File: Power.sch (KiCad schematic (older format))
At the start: 35 parts, among them IC4 INA240A1, IC5 INA240A1, U2 IR2110S, U3 IR2110S, U4 IR2110S

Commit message: - removed 1 MOSFET of each group (no space) - removed 2 DC buffer caps (no space) - power stage routed - shunts and amps routed - post driver routed - pre driver HV routed
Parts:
- removed IC4, IC5: INA240A1, Housings_SSOP:TSSOP-8_4.4x3mm_Pitch0.65mm, symbol INA240
- removed R49, R50, R51, R52: opt, Resistors_SMD:R_0805, symbol R
- added D10, D11, D12: 3V3, Diodes_SMD:D_SOD-123, symbol ZENER
- added IC3, IC4: INA181A1, TO_SOT_Packages_SMD:SOT-23-6, symbol INA181
- added R45, R46: 10k, Resistors_SMD:R_0805, symbol R
- C40, C42: value opt -> 100n
- D5, D6, D7: value RFN2L4S -> BAS21L; footprint Diodes_SMD:SMA_Standard -> Diodes_SMD:D_SOT-23_ANK
- R47, R48: value CSS2H-3920R-L500 -> WSLF2512L5000FEB
- U2, U3, U4: footprint Housings_SOIC:SOIC-16_7.5x10.3mm_Pitch1.27mm -> Housings_SOIC:SOIC-16W_7.5x10.3mm_Pitch1.27mm
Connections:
- net labels added: U/2
- wire segments 79 -> 88
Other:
- moved on the sheet: R55, R56, R57, R58

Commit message: - fixed swapped pins 2 and 3 on IC2 - added optional dividers to ADC inputs - made Vcc selectable between 3V3 or 5V
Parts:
- D10, D11, D12: symbol ZENER -> ZENER-RESCUE-Revolter
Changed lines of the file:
@@
 $EndComp
 $Comp
-L GND-RESCUE-BLDC_4 #PWR072
+L GND-RESCUE-BLDC_4 #PWR075
 U 1 1 504F8F7B
 P 10400 1300
-F 0 "#PWR072" H 10400 1300 30  0001 C CNN
+F 0 "#PWR075" H 10400 1300 30  0001 C CNN
 F 1 "GND" H 10400 1230 30  0001 C CNN
 F 2 "" H 10400 1300 60  0001 C CNN
@@
 $EndComp
 $Comp
-L GND-RESCUE-BLDC_4 #PWR073
+L GND-RESCUE-BLDC_4 #PWR076
 U 1 1 504F8F8D
 P 10400 2000
-F 0 "#PWR073" H 10400 2000 30  0001 C CNN
+F 0 "#PWR076" H 10400 2000 30  0001 C CNN
 F 1 "GND" H 10400 1930 30  0001 C CNN
 F 2 "" H 10400 2000 60  0001 C CNN
@@
 $EndComp
 $Comp
-L GND-RESCUE-BLDC_4 #PWR074
+L GND-RESCUE-BLDC_4 #PWR077
 U 1 1 504F8FAF
 P 10400 2700
-F 0 "#PWR074" H 10400 2700 30  0001 C CNN
+F 0 "#PWR077" H 10400 2700 30  0001 C CNN
 F 1 "GND" H 10400 2630 30  0001 C CNN
 F 2 "" H 10400 2700 60  0001 C CNN
@@
 $EndComp
 $Comp
-L +12V #PWR075
+L +12V #PWR078
 U 1 1 574ED597
 P 2500 900
-F 0 "#PWR075" H 2500 750 50  0001 C CNN
+F 0 "#PWR078" H 2500 750 50  0001 C CNN
 F 1 "+12V" H 2500 1040 50  0000 C CNN
 F 2 "" H 2500 900 50  0000 C CNN
@@
 $EndComp
 $Comp
-L GND #PWR076
+L GND #PWR079
 U 1 1 574EDDD7
 P 1850 1050
-F 0 "#PWR076" H 1850 800 50  0001 C CNN
+F 0 "#PWR079" H 1850 800 50  0001 C CNN
 F 1 "GND" H 1850 900 50  0000 C CNN
 F 2 "" H 1850 1050 50  0000 C CNN
@@
 $EndComp
 $Comp
-L GND #PWR077
+L GND #PWR080
 U 1 1 574F0470
 P 2200 2300
-F 0 "#PWR077" H 2200 2050 50  0001 C CNN
+F 0 "#PWR080" H 2200 2050 50  0001 C CNN
 F 1 "GND" H 2200 2150 50  0000 C CNN
 F 2 "" H 2200 2300 50  0000 C CNN
@@
 $EndComp
 $Comp
-L +12V #PWR078
+L +12V #PWR081
 U 1 1 57504386
 P 2500 3200
-F 0 "#PWR078" H 2500 3050 50  0001 C CNN
+F 0 "#PWR081" H 2500 3050 50  0001 C CNN
 F 1 "+12V" H 2500 3340 50  0000 C CNN
 F 2 "" H 2500 3200 50  0000 C CNN
@@
 $EndComp
 $Comp
-L GND #PWR079
+L GND #PWR082
 U 1 1 5750439C
 P 1850 3350
-F 0 "#PWR079" H 1850 3100 50  0001 C CNN
+F 0 "#PWR082" H 1850 3100 50  0001 C CNN
 F 1 "GND" H 1850 3200 50  0000 C CNN
 F 2 "" H 1850 3350 50  0000 C CNN
@@
 $EndComp
 $Comp
-L GND #PWR080
+L GND #PWR083
 U 1 1 575043A3
 P 2200 4600
-F 0 "#PWR080" H 2200 4350 50  0001 C CNN
+F 0 "#PWR083" H 2200 4350 50  0001 C CNN
 F 1 "GND" H 2200 4450 50  0000 C CNN
 F 2 "" H 2200 4600 50  0000 C CNN
@@
 $EndComp
 $Comp
-L +12V #PWR081
+L +12V #PWR084
 U 1 1 57504606
 P 2450 5350
-F 0 "#PWR081" H 2450 5200 50  0001 C CNN
+F 0 "#PWR084" H 2450 5200 50  0001 C CNN
 F 1 "+12V" H 2450 5490 50  0000 C CNN
 F 2 "" H 2450 5350 50  0000 C CNN
@@
 $EndComp
 $Comp
-L GND #PWR082
+L GND #PWR085
 U 1 1 5750461C
 P 1800 5500
-F 0 "#PWR082" H 1800 5250 50  0001 C CNN
+F 0 "#PWR085" H 1800 5250 50  0001 C CNN
 F 1 "GND" H 1800 5350 50  0000 C CNN
 F 2 "" H 1800 5500 50  0000 C CNN
@@
 $EndComp
 $Comp
-L GND #PWR083
+L GND #PWR086
 U 1 1 57504623
 P 2150 6750
-F 0 "#PWR083" H 2150 6500 50  0001 C CNN
+F 0 "#PWR086" H 2150 6500 50  0001 C CNN
 F 1 "GND" H 2150 6600 50  0000 C CNN
 F 2 "" H 2150 6750 50  0000 C CNN
@@
 H2_VS
 $Comp
-L +3V3 #PWR084
+L +3V3 #PWR087
 U 1 1 575461AA
 P 2200 900
-F 0 "#PWR084" H 2200 750 50  0001 C CNN
+F 0 "#PWR087" H 2200 750 50  0001 C CNN
 F 1 "+3V3" H 2200 1040 50  0000 C CNN
 F 2 "" H 2200 900 50  0000 C CNN
@@
 $EndComp
 $Comp
-L +3V3 #PWR085
+L +3V3 #PWR088
 U 1 1 575462A0
 P 2200 3200
-F 0 "#PWR085" H 2200 3050 50  0001 C CNN
+F 0 "#PWR088" H 2200 3050 50  0001 C CNN
 F 1 "+3V3" H 2200 3340 50  0000 C CNN
 F 2 "" H 2200 3200 50  0000 C CNN
@@
 $EndComp
 $Comp
-L +3V3 #PWR086
+L +3V3 #PWR089
 U 1 1 57546CC3
 P 2150 5350
-F 0 "#PWR086" H 2150 5200 50  0001 C CNN
+F 0 "#PWR089" H 2150 5200 50  0001 C CNN
 F 1 "+3V3" H 2150 5490 50  0000 C CNN
 F 2 "" H 2150 5350 50  0000 C CNN
@@
 $EndComp
 $Comp
-L GNDPWR #PWR087
+L GNDPWR #PWR090
 U 1 1 58976189
 P 4150 2800
-F 0 "#PWR087" H 4150 2600 50  0001 C CNN
+F 0 "#PWR090" H 4150 2600 50  0001 C CNN
 F 1 "GNDPWR" H 4150 2670 50  0000 C CNN
 F 2 "" H 4150 2750 50  0000 C CNN
@@
 $EndComp
 $Comp
-L GND-RESCUE-BLDC_4 #PWR088
+L GND-RESCUE-BLDC_4 #PWR091
 U 1 1 5897662E
 P 5050 3000
-F 0 "#PWR088" H 5050 3000 30  0001 C CNN
+F 0 "#PWR091" H 5050 3000 30  0001 C CNN
 F 1 "GND" H 5050 2930 30  0001 C CNN
 F 2 "" H 5050 3000 60  0001 C CNN
@@
 $EndComp
 $Comp
-L +3V3 #PWR089
+L +3V3 #PWR092
 U 1 1 58977A83
 P 4450 1850
-F 0 "#PWR089" H 4450 1700 50  0001 C CNN
+F 0 "#PWR092" H 4450 1700 50  0001 C CNN
 F 1 "+3V3" H 4450 1990 50  0000 C CNN
 F 2 "" H 4450 1850 50  0000 C CNN
@@
 $EndComp
 $Comp
-L GND-RESCUE-BLDC_4 #PWR090
+L GND-RESCUE-BLDC_4 #PWR093
 U 1 1 58978042
 P 4450 2150
-F 0 "#PWR090" H 4450 2150 30  0001 C CNN
+F 0 "#PWR093" H 4450 2150 30  0001 C CNN
 F 1 "GND" H 4450 2080 30  0001 C CNN
 F 2 "" H 4450 2150 60  0001 C CNN
@@
 $EndComp
 $Comp
-L GND-RESCUE-BLDC_4 #PWR091
+L GND-RESCUE-BLDC_4 #PWR094
 U 1 1 589781C4
 P 4700 2150
-F 0 "#PWR091" H 4700 2150 30  0001 C CNN
+F 0 "#PWR094" H 4700 2150 30  0001 C CNN
 F 1 "GND" H 4700 2080 30  0001 C CNN
 F 2 "" H 4700 2150 60  0001 C CNN
@@
 $EndComp
 $Comp
-L GNDPWR #PWR092
+L GNDPWR #PWR095
 U 1 1 58979499
 P 4100 7250
-F 0 "#PWR092" H 4100 7050 50  0001 C CNN
+F 0 "#PWR095" H 4100 7050 50  0001 C CNN
 F 1 "GNDPWR" H 4100 7120 50  0000 C CNN
 F 2 "" H 4100 7200 50  0000 C CNN
@@
 $EndComp
 $Comp
-L GND-RESCUE-BLDC_4 #PWR093
+L GND-RESCUE-BLDC_4 #PWR096
 U 1 1 589794A0
 P 5000 7450
-F 0 "#PWR093" H 5000 7450 30  0001 C CNN
+F 0 "#PWR096" H 5000 7450 30  0001 C CNN
 F 1 "GND" H 5000 7380 30  0001 C CNN
 F 2 "" H 5000 7450 60  0001 C CNN
@@
 $EndComp
 $Comp
-L +3V3 #PWR094
+L +3V3 #PWR097
 U 1 1 589794AC
 P 4400 6300
-F 0 "#PWR094" H 4400 6150 50  0001 C CNN
+F 0 "#PWR097" H 4400 6150 50  0001 C CNN
 F 1 "+3V3" H 4400 6440 50  0000 C CNN
 F 2 "" H 4400 6300 50  0000 C CNN
@@
 $EndComp
 $Comp
-L GND-RESCUE-BLDC_4 #PWR095
+L GND-RESCUE-BLDC_4 #PWR098
 U 1 1 589794BE
 P 4400 6600
-F 0 "#PWR095" H 4400 6600 30  0001 C CNN
+F 0 "#PWR098" H 4400 6600 30  0001 C CNN
 F 1 "GND" H 4400 6530 30  0001 C CNN
 F 2 "" H 4400 6600 60  0001 C CNN
@@
 $EndComp
 $Comp
-L GND-RESCUE-BLDC_4 #PWR096
+L GND-RESCUE-BLDC_4 #PWR099
 U 1 1 589794C4
 P 4650 6600
-F 0 "#PWR096" H 4650 6600 30  0001 C CNN
+F 0 "#PWR099" H 4650 6600 30  0001 C CNN
 F 1 "GND" H 4650 6530 30  0001 C CNN
 F 2 "" H 4650 6600 60  0001 C CNN
@@
 BR_SO1
 $Comp
-L GNDPWR #PWR097
+L GNDPWR #PWR0100
 U 1 1 58985697
 P 4150 4700
-F 0 "#PWR097" H 4150 4500 50  0001 C CNN
+F 0 "#PWR0100" H 4150 4500 50  0001 C CNN
 F 1 "GNDPWR" H 4150 4570 50  0000 C CNN
 F 2 "" H 4150 4650 50  0000 C CNN
@@
 $EndComp
 $Comp
-L ZENER D10
+L ZENER-RESCUE-Revolter D10
 U 1 1 599A646A
 P 9900 1550
@@
 $EndComp
 $Comp
-L ZENER D11
+L ZENER-RESCUE-Revolter D11
 U 1 1 599A6EDF
 P 9900 2250
@@
 $EndComp
 $Comp
-L ZENER D12
+L ZENER-RESCUE-Revolter D12
 U 1 1 599A735E
 P 9900 2950
@@
 Connection ~ 5750 2700
 $Comp
-L GND-RESCUE-BLDC_4 #PWR098
+L GND-RESCUE-BLDC_4 #PWR0101
 U 1 1 59A0D35D
 P 5750 3000
-F 0 "#PWR098" H 5750 3000 30  0001 C CNN
+F 0 "#PWR0101" H 5750 3000 30  0001 C CNN
 F 1 "GND" H 5750 2930 30  0001 C CNN
 F 2 "" H 5750 3000 60  0001 C CNN
@@
 $EndComp
 $Comp
-L GND-RESCUE-BLDC_4 #PWR099
+L GND-RESCUE-BLDC_4 #PWR0102
 U 1 1 59A0DC28
 P 6000 3000
-F 0 "#PWR099" H 6000 3000 30  0001 C CNN
+F 0 "#PWR0102" H 6000 3000 30  0001 C CNN
 F 1 "GND" H 6000 2930 30  0001 C CNN
 F 2 "" H 6000 3000 60  0001 C CNN
@@
 $EndComp
 $Comp
-L GND-RESCUE-BLDC_4 #PWR0100
+L GND-RESCUE-BLDC_4 #PWR0103
 U 1 1 59A0ED1B
 P 5500 7450
-F 0 "#PWR0100" H 5500 7450 30  0001 C CNN
+F 0 "#PWR0103" H 5500 7450 30  0001 C CNN
 F 1 "GND" H 5500 7380 30  0001 C CNN
 F 2 "" H 5500 7450 60  0001 C CNN

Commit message: - basis commit for V1.1 - did an great overhaul of high current paths - fixed wrong 3V3 reg pin out - blew the IO connector up to 8 pins (turns out 7pin is rare) - changed shunt to 2512 - changed hf caps to double 1210 - two input caps - pin outs for all IO on silk screen - spread the references so you can actually read them - connected the Hall/Temp pull-ups to 3V3 instead of 5V - changed vias to 0.6/0.3mm - changed text to V1.1
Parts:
- R47, R48: footprint alexmod:CSS3920 -> Resistors_SMD:R_2512
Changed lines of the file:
@@
 $EndComp
 $Comp
-L GND-RESCUE-BLDC_4 #PWR075
+L GND-RESCUE-BLDC_4 #PWR076
 U 1 1 504F8F7B
 P 10400 1300
-F 0 "#PWR075" H 10400 1300 30  0001 C CNN
+F 0 "#PWR076" H 10400 1300 30  0001 C CNN
 F 1 "GND" H 10400 1230 30  0001 C CNN
 F 2 "" H 10400 1300 60  0001 C CNN
@@
 $EndComp
 $Comp
-L GND-RESCUE-BLDC_4 #PWR076
+L GND-RESCUE-BLDC_4 #PWR077
 U 1 1 504F8F8D
 P 10400 2000
-F 0 "#PWR076" H 10400 2000 30  0001 C CNN
+F 0 "#PWR077" H 10400 2000 30  0001 C CNN
 F 1 "GND" H 10400 1930 30  0001 C CNN
 F 2 "" H 10400 2000 60  0001 C CNN
@@
 $EndComp
 $Comp
-L GND-RESCUE-BLDC_4 #PWR077
+L GND-RESCUE-BLDC_4 #PWR078
 U 1 1 504F8FAF
 P 10400 2700
-F 0 "#PWR077" H 10400 2700 30  0001 C CNN
+F 0 "#PWR078" H 10400 2700 30  0001 C CNN
 F 1 "GND" H 10400 2630 30  0001 C CNN
 F 2 "" H 10400 2700 60  0001 C CNN
@@
 $EndComp
 $Comp
-L +12V #PWR078
+L +12V #PWR079
 U 1 1 574ED597
 P 2500 900
-F 0 "#PWR078" H 2500 750 50  0001 C CNN
+F 0 "#PWR079" H 2500 750 50  0001 C CNN
 F 1 "+12V" H 2500 1040 50  0000 C CNN
 F 2 "" H 2500 900 50  0000 C CNN
@@
 $EndComp
 $Comp
-L GND #PWR079
+L GND #PWR080
 U 1 1 574EDDD7
 P 1850 1050
-F 0 "#PWR079" H 1850 800 50  0001 C CNN
+F 0 "#PWR080" H 1850 800 50  0001 C CNN
 F 1 "GND" H 1850 900 50  0000 C CNN
 F 2 "" H 1850 1050 50  0000 C CNN
@@
 $EndComp
 $Comp
-L GND #PWR080
+L GND #PWR081
 U 1 1 574F0470
 P 2200 2300
-F 0 "#PWR080" H 2200 2050 50  0001 C CNN
+F 0 "#PWR081" H 2200 2050 50  0001 C CNN
 F 1 "GND" H 2200 2150 50  0000 C CNN
 F 2 "" H 2200 2300 50  0000 C CNN
@@
 $EndComp
 $Comp
-L +12V #PWR081
+L +12V #PWR082
 U 1 1 57504386
 P 2500 3200
-F 0 "#PWR081" H 2500 3050 50  0001 C CNN
+F 0 "#PWR082" H 2500 3050 50  0001 C CNN
 F 1 "+12V" H 2500 3340 50  0000 C CNN
 F 2 "" H 2500 3200 50  0000 C CNN
@@
 $EndComp
 $Comp
-L GND #PWR082
+L GND #PWR083
 U 1 1 5750439C
 P 1850 3350
-F 0 "#PWR082" H 1850 3100 50  0001 C CNN
+F 0 "#PWR083" H 1850 3100 50  0001 C CNN
 F 1 "GND" H 1850 3200 50  0000 C CNN
 F 2 "" H 1850 3350 50  0000 C CNN
@@
 $EndComp
 $Comp
-L GND #PWR083
+L GND #PWR084
 U 1 1 575043A3
 P 2200 4600
-F 0 "#PWR083" H 2200 4350 50  0001 C CNN
+F 0 "#PWR084" H 2200 4350 50  0001 C CNN
 F 1 "GND" H 2200 4450 50  0000 C CNN
 F 2 "" H 2200 4600 50  0000 C CNN
@@
 $EndComp
 $Comp
-L +12V #PWR084
+L +12V #PWR085
 U 1 1 57504606
 P 2450 5350
-F 0 "#PWR084" H 2450 5200 50  0001 C CNN
+F 0 "#PWR085" H 2450 5200 50  0001 C CNN
 F 1 "+12V" H 2450 5490 50  0000 C CNN
 F 2 "" H 2450 5350 50  0000 C CNN
@@
 $EndComp
 $Comp
-L GND #PWR085
+L GND #PWR086
 U 1 1 5750461C
 P 1800 5500
-F 0 "#PWR085" H 1800 5250 50  0001 C CNN
+F 0 "#PWR086" H 1800 5250 50  0001 C CNN
 F 1 "GND" H 1800 5350 50  0000 C CNN
 F 2 "" H 1800 5500 50  0000 C CNN
@@
 $EndComp
 $Comp
-L GND #PWR086
+L GND #PWR087
 U 1 1 57504623
 P 2150 6750
-F 0 "#PWR086" H 2150 6500 50  0001 C CNN
+F 0 "#PWR087" H 2150 6500 50  0001 C CNN
 F 1 "GND" H 2150 6600 50  0000 C CNN
 F 2 "" H 2150 6750 50  0000 C CNN
@@
 H2_VS
 $Comp
-L +3V3 #PWR087
+L +3V3 #PWR088
 U 1 1 575461AA
 P 2200 900
-F 0 "#PWR087" H 2200 750 50  0001 C CNN
+F 0 "#PWR088" H 2200 750 50  0001 C CNN
 F 1 "+3V3" H 2200 1040 50  0000 C CNN
 F 2 "" H 2200 900 50  0000 C CNN
@@
 $EndComp
 $Comp
-L +3V3 #PWR088
+L +3V3 #PWR089
 U 1 1 575462A0
 P 2200 3200
-F 0 "#PWR088" H 2200 3050 50  0001 C CNN
+F 0 "#PWR089" H 2200 3050 50  0001 C CNN
 F 1 "+3V3" H 2200 3340 50  0000 C CNN
 F 2 "" H 2200 3200 50  0000 C CNN
@@
 $EndComp
 $Comp
-L +3V3 #PWR089
+L +3V3 #PWR090
 U 1 1 57546CC3
 P 2150 5350
-F 0 "#PWR089" H 2150 5200 50  0001 C CNN
+F 0 "#PWR090" H 2150 5200 50  0001 C CNN
 F 1 "+3V3" H 2150 5490 50  0000 C CNN
 F 2 "" H 2150 5350 50  0000 C CNN
@@
 F 0 "R48" V 4230 2550 50  0000 C CNN
 F 1 "WSLF2512L5000FEB" V 4350 2750 50  0000 C CNN
-F 2 "alexmod:CSS3920" V 4080 2550 50  0001 C CNN
+F 2 "Resistors_SMD:R_2512" V 4080 2550 50  0001 C CNN
 F 3 "" H 4150 2550 50  0000 C CNN
 	1    4150 2550
@@
 $EndComp
 $Comp
-L GNDPWR #PWR090
+L GNDPWR #PWR091
 U 1 1 58976189
 P 4150 2800
-F 0 "#PWR090" H 4150 2600 50  0001 C CNN
+F 0 "#PWR091" H 4150 2600 50  0001 C CNN
 F 1 "GNDPWR" H 4150 2670 50  0000 C CNN
 F 2 "" H 4150 2750 50  0000 C CNN
@@
 $EndComp
 $Comp
-L GND-RESCUE-BLDC_4 #PWR091
+L GND-RESCUE-BLDC_4 #PWR092
 U 1 1 5897662E
 P 5050 3000
-F 0 "#PWR091" H 5050 3000 30  0001 C CNN
+F 0 "#PWR092" H 5050 3000 30  0001 C CNN
 F 1 "GND" H 5050 2930 30  0001 C CNN
 F 2 "" H 5050 3000 60  0001 C CNN
@@
 $EndComp
 $Comp
-L +3V3 #PWR092
+L +3V3 #PWR093
 U 1 1 58977A83
 P 4450 1850
-F 0 "#PWR092" H 4450 1700 50  0001 C CNN
+F 0 "#PWR093" H 4450 1700 50  0001 C CNN
 F 1 "+3V3" H 4450 1990 50  0000 C CNN
 F 2 "" H 4450 1850 50  0000 C CNN
@@
 $EndComp
 $Comp
-L GND-RESCUE-BLDC_4 #PWR093
+L GND-RESCUE-BLDC_4 #PWR094
 U 1 1 58978042
 P 4450 2150
-F 0 "#PWR093" H 4450 2150 30  0001 C CNN
+F 0 "#PWR094" H 4450 2150 30  0001 C CNN
 F 1 "GND" H 4450 2080 30  0001 C CNN
 F 2 "" H 4450 2150 60  0001 C CNN
@@
 $EndComp
 $Comp
-L GND-RESCUE-BLDC_4 #PWR094
+L GND-RESCUE-BLDC_4 #PWR095
 U 1 1 589781C4
 P 4700 2150
-F 0 "#PWR094" H 4700 2150 30  0001 C CNN
+F 0 "#PWR095" H 4700 2150 30  0001 C CNN
 F 1 "GND" H 4700 2080 30  0001 C CNN
 F 2 "" H 4700 2150 60  0001 C CNN
@@
 F 0 "R47" V 4180 7000 50  0000 C CNN
 F 1 "WSLF2512L5000FEB" V 4350 7200 50  0000 C CNN
-F 2 "alexmod:CSS3920" V 4030 7000 50  0001 C CNN
+F 2 "Resistors_SMD:R_2512" V 4030 7000 50  0001 C CNN
 F 3 "" H 4100 7000 50  0000 C CNN
 	1    4100 7000
@@
 $EndComp
 $Comp
-L GNDPWR #PWR095
+L GNDPWR #PWR096
 U 1 1 58979499
 P 4100 7250
-F 0 "#PWR095" H 4100 7050 50  0001 C CNN
+F 0 "#PWR096" H 4100 7050 50  0001 C CNN
 F 1 "GNDPWR" H 4100 7120 50  0000 C CNN
 F 2 "" H 4100 7200 50  0000 C CNN
@@
 $EndComp
 $Comp
-L GND-RESCUE-BLDC_4 #PWR096
+L GND-RESCUE-BLDC_4 #PWR097
 U 1 1 589794A0
 P 5000 7450
-F 0 "#PWR096" H 5000 7450 30  0001 C CNN
+F 0 "#PWR097" H 5000 7450 30  0001 C CNN
 F 1 "GND" H 5000 7380 30  0001 C CNN
 F 2 "" H 5000 7450 60  0001 C CNN
@@
 $EndComp
 $Comp
-L +3V3 #PWR097
+L +3V3 #PWR098
 U 1 1 589794AC
 P 4400 6300
-F 0 "#PWR097" H 4400 6150 50  0001 C CNN
+F 0 "#PWR098" H 4400 6150 50  0001 C CNN
 F 1 "+3V3" H 4400 6440 50  0000 C CNN
 F 2 "" H 4400 6300 50  0000 C CNN
@@
 $EndComp
 $Comp
-L GND-RESCUE-BLDC_4 #PWR098
+L GND-RESCUE-BLDC_4 #PWR099
 U 1 1 589794BE
 P 4400 6600
-F 0 "#PWR098" H 4400 6600 30  0001 C CNN
+F 0 "#PWR099" H 4400 6600 30  0001 C CNN
 F 1 "GND" H 4400 6530 30  0001 C CNN
 F 2 "" H 4400 6600 60  0001 C CNN
@@
 $EndComp
 $Comp
-L GND-RESCUE-BLDC_4 #PWR099
+L GND-RESCUE-BLDC_4 #PWR0100
 U 1 1 589794C4
 P 4650 6600
-F 0 "#PWR099" H 4650 6600 30  0001 C CNN
+F 0 "#PWR0100" H 4650 6600 30  0001 C CNN
 F 1 "GND" H 4650 6530 30  0001 C CNN
 F 2 "" H 4650 6600 60  0001 C CNN
@@
 BR_SO1
 $Comp
-L GNDPWR #PWR0100
+L GNDPWR #PWR0101
 U 1 1 58985697
 P 4150 4700
-F 0 "#PWR0100" H 4150 4500 50  0001 C CNN
+F 0 "#PWR0101" H 4150 4500 50  0001 C CNN
 F 1 "GNDPWR" H 4150 4570 50  0000 C CNN
 F 2 "" H 4150 4650 50  0000 C CNN
@@
 Connection ~ 5750 2700
 $Comp
-L GND-RESCUE-BLDC_4 #PWR0101
+L GND-RESCUE-BLDC_4 #PWR0102
 U 1 1 59A0D35D
 P 5750 3000
-F 0 "#PWR0101" H 5750 3000 30  0001 C CNN
+F 0 "#PWR0102" H 5750 3000 30  0001 C CNN
 F 1 "GND" H 5750 2930 30  0001 C CNN
 F 2 "" H 5750 3000 60  0001 C CNN
@@
 $EndComp
 $Comp
-L GND-RESCUE-BLDC_4 #PWR0102
+L GND-RESCUE-BLDC_4 #PWR0103
 U 1 1 59A0DC28
 P 6000 3000
-F 0 "#PWR0102" H 6000 3000 30  0001 C CNN
+F 0 "#PWR0103" H 6000 3000 30  0001 C CNN
 F 1 "GND" H 6000 2930 30  0001 C CNN
 F 2 "" H 6000 3000 60  0001 C CNN
@@
 $EndComp
 $Comp
-L GND-RESCUE-BLDC_4 #PWR0103
+L GND-RESCUE-BLDC_4 #PWR0104
 U 1 1 59A0ED1B
 P 5500 7450
-F 0 "#PWR0103" H 5500 7450 30  0001 C CNN
+F 0 "#PWR0104" H 5500 7450 30  0001 C CNN
 F 1 "GND" H 5500 7380 30  0001 C CNN
 F 2 "" H 5500 7450 60  0001 C CNN

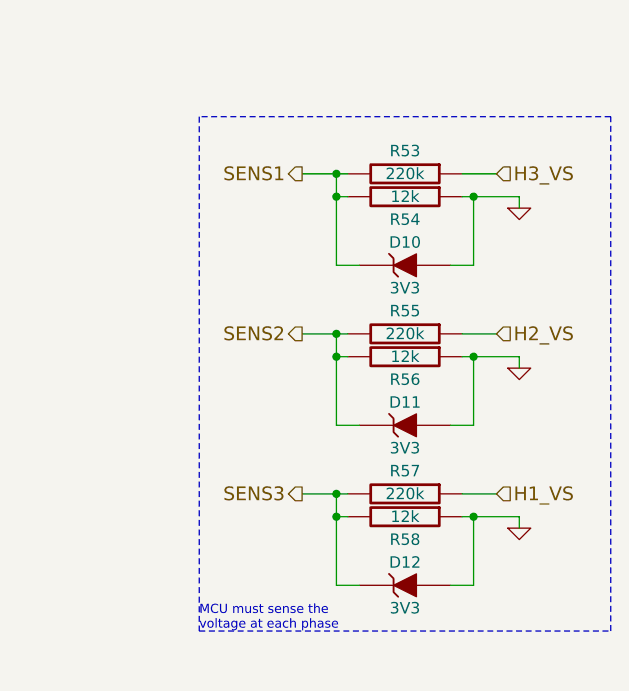
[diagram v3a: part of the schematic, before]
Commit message: - changed dividers to 100k vs 3k3
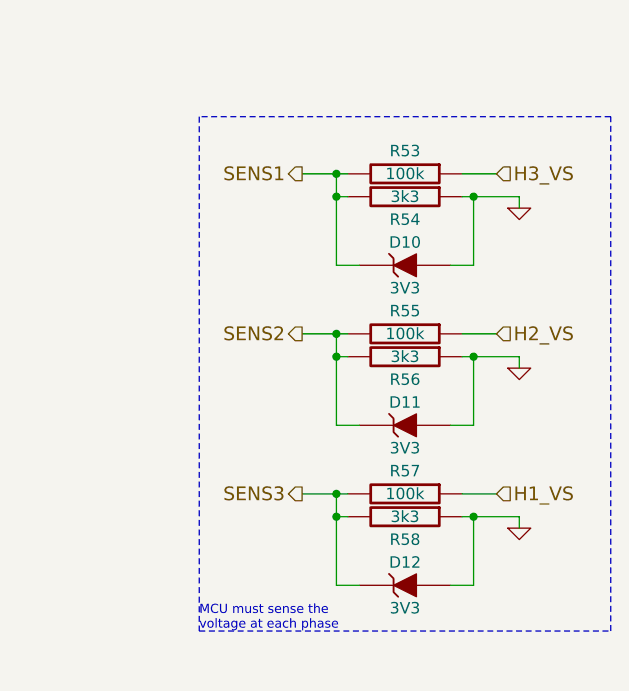
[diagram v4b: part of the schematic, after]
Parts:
- R53, R55, R57: value 220k -> 100k
- R54, R56, R58: value 12k -> 3k3
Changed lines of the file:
@@
 P 9900 1150
 F 0 "R53" V 9800 1150 50  0000 C CNN
-F 1 "220k" V 9900 1150 50  0000 C CNN
+F 1 "100k" V 9900 1150 50  0000 C CNN
 F 2 "Resistors_SMD:R_0805" H 9900 1150 60  0001 C CNN
 F 3 "" H 9900 1150 60  0001 C CNN
@@
 P 9900 1250
 F 0 "R54" V 10000 1250 50  0000 C CNN
-F 1 "12k" V 9900 1250 50  0000 C CNN
+F 1 "3k3" V 9900 1250 50  0000 C CNN
 F 2 "Resistors_SMD:R_0805" H 9900 1250 60  0001 C CNN
 F 3 "" H 9900 1250 60  0001 C CNN
@@
 P 9900 1950
 F 0 "R56" V 10000 1950 50  0000 C CNN
-F 1 "12k" V 9900 1950 50  0000 C CNN
+F 1 "3k3" V 9900 1950 50  0000 C CNN
 F 2 "Resistors_SMD:R_0805" H 9900 1950 60  0001 C CNN
 F 3 "" H 9900 1950 60  0001 C CNN
@@
 P 9900 1850
 F 0 "R55" V 9800 1850 50  0000 C CNN
-F 1 "220k" V 9900 1850 50  0000 C CNN
+F 1 "100k" V 9900 1850 50  0000 C CNN
 F 2 "Resistors_SMD:R_0805" H 9900 1850 60  0001 C CNN
 F 3 "" H 9900 1850 60  0001 C CNN
@@
 P 9900 2550
 F 0 "R57" V 9800 2550 50  0000 C CNN
-F 1 "220k" V 9900 2550 50  0000 C CNN
+F 1 "100k" V 9900 2550 50  0000 C CNN
 F 2 "Resistors_SMD:R_0805" H 9900 2550 60  0001 C CNN
 F 3 "" H 9900 2550 60  0001 C CNN
@@
 P 9900 2650
 F 0 "R58" V 10000 2650 50  0000 C CNN
-F 1 "12k" V 9900 2650 50  0000 C CNN
+F 1 "3k3" V 9900 2650 50  0000 C CNN
 F 2 "Resistors_SMD:R_0805" H 9900 2650 60  0001 C CNN
 F 3 "" H 9900 2650 60  0001 C CNN

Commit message: - updated project to 5.0.0 - added some more ignores
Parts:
- C33, C34, C35, C36, C37, C38, C59, C60, C61: symbol C_Small -> Device:C_Small
- C39, C40, C41, C42, C43, C44: symbol C -> Device:C
- D10, D11, D12: symbol ZENER-RESCUE-Revolter -> Revolter-rescue:ZENER-RESCUE-Revolter
- D5, D6, D7: symbol D_Small -> Device:D_Small
- IC3, IC4: symbol INA181 -> Revolter-rescue:INA181
- R45, R46, R47, R48: symbol R -> Device:R
- R53, R54, R55, R56, R57, R58: symbol R-RESCUE-BLDC_4 -> Revolter-rescue:R-RESCUE-BLDC_4
- U2, U3, U4: symbol IR2110S -> Revolter-rescue:IR2110S

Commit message: - swapped TO220 dual MOSFET for single DualCool88 MOSFET package - removed postdriver - changed IRS2110 for IRS2186 - added third shunt - rewired CPU for VESC6 compatibility - layout completely from scratch
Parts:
- removed C33, C34, C35, C36, C37, C38, C59, C60, C61: 100n, Capacitors_SMD:C_0805, symbol Device:C_Small
- removed D7: BAS21L, Diodes_SMD:D_SOT-23_ANK, symbol Device:D_Small
- removed U2, U3, U4: IR2110S, Housings_SOIC:SOIC-16W_7.5x10.3mm_Pitch1.27mm, symbol Revolter-rescue:IR2110S
- added C33, C35, C4, C5, C6, C7, C8: 1u, Capacitor_SMD:C_0805_2012Metric, symbol Device:C
- added C34: 10n, Capacitor_SMD:C_0805_2012Metric, symbol Device:C
- added C36: 100n, Capacitor_SMD:C_0805_2012Metric, symbol Device:C
- added D1: BAS21L, Diode_SMD:D_SOT-23_ANK, symbol Device:D_Small
- added IC5: INA181A1, Package_TO_SOT_SMD:SOT-23-6, symbol Revolter-rescue:INA181
- added R3: WSLF2512L5000FEB, Resistor_SMD:R_2512_6332Metric, symbol Device:R
- added U2, U3, U4: IRS2186, Package_SO:SO-8_3.9x4.9mm_P1.27mm, symbol Driver_FET:IRS2186
- C39, C40, C41, C42, C43, C44: footprint Capacitors_SMD:C_0805 -> Capacitor_SMD:C_0805_2012Metric
- D10, D11, D12: footprint Diodes_SMD:D_SOD-123 -> Diode_SMD:D_SOD-123
- D5, D6: footprint Diodes_SMD:D_SOT-23_ANK -> Diode_SMD:D_SOT-23_ANK
- IC3, IC4: footprint TO_SOT_Packages_SMD:SOT-23-6 -> Package_TO_SOT_SMD:SOT-23-6
- R45, R46, R53, R54, R55, R56, R57, R58: footprint Resistors_SMD:R_0805 -> Resistor_SMD:R_0805_2012Metric
- R47, R48: footprint Resistors_SMD:R_2512 -> Resistor_SMD:R_2512_6332Metric
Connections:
- net labels added: CURRENT_1, CURRENT_2, CURRENT_3, VOLTAGE_1, VOLTAGE_2, VOLTAGE_3
- net labels removed: BR_SO1, BR_SO2, EN_GATE, H1_HI, H1_VL, H2_HI, H2_VL, H3_HI, H3_VL, SENS1, SENS2, SENS3
- wire segments 88 -> 91
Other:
- moved on the sheet: C39, C40, C41, C42, C43, C44, D6, IC3, IC4, R45, R46, R47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
